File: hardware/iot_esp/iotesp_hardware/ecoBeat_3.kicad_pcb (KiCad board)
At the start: 2 copper layers, 67.6 x 58.6 mm, 10 parts, among them J1 Test, P1 CONN_02X05, U1 WeMos_mini

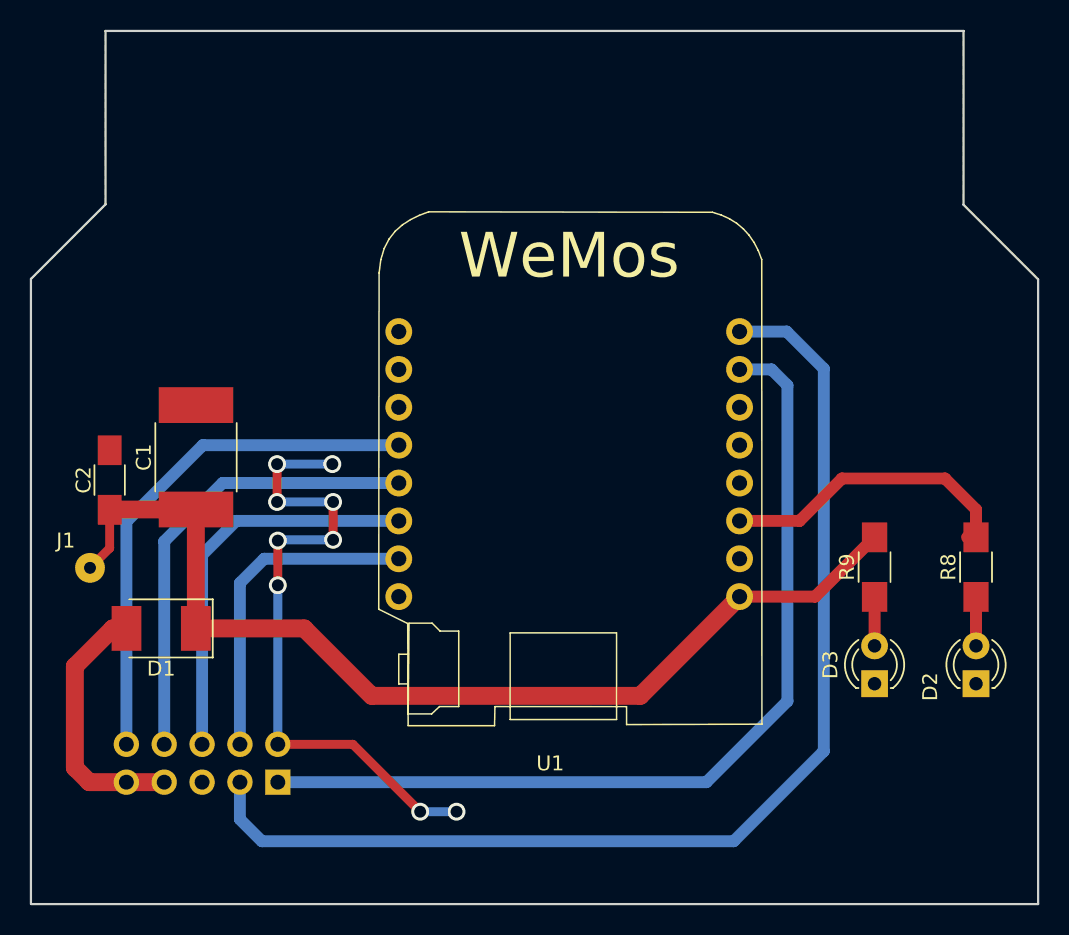
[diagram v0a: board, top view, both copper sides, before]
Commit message: iot-esp hw v3: side ventilation
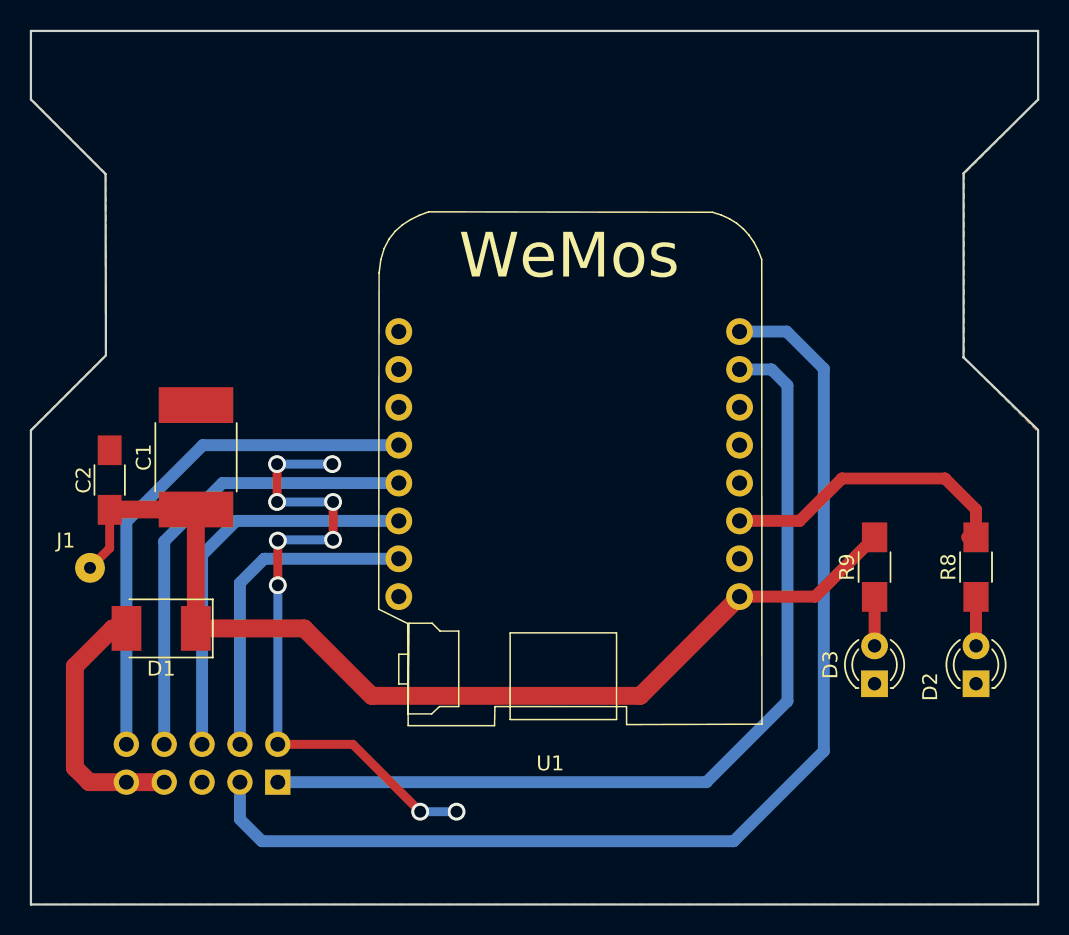
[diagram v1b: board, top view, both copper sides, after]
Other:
- outline, holes or cut-outs redrawn
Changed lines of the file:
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@@
-(kicad_pcb (version 4) (host pcbnew 4.0.7-e2-6376~61~ubuntu18.04.1)
+(kicad_pcb (version 20171130) (host pcbnew 5.0.2+dfsg1-1)
   (general
-    (links 22)
-    (no_connects 0)
-    (area 28.014801 19.652 132.9196 109.329201)
     (thickness 1.6)
-    (drawings 29)
+    (drawings 36)
     (tracks 72)
     (zones 0)
@@
   )
   (layers
-    (0 F.Cu signal hide)
-    (31 B.Cu signal hide)
+    (0 F.Cu signal)
+    (31 B.Cu signal)
     (32 B.Adhes user)
     (33 F.Adhes user)
@@
     (42 Eco1.User user)
     (43 Eco2.User user)
-    (44 Edge.Cuts user)
+    (44 Edge.Cuts user hide)
     (45 Margin user)
     (46 B.CrtYd user)
@@
     (pad_drill 1)
     (pad_to_mask_clearance 0.2)
+    (solder_mask_min_width 0.25)
     (aux_axis_origin 0 0)
     (grid_origin 221.6404 115.9764)
@@
       (layerselection 0x3d0f0_80000001)
       (usegerberextensions false)
+      (usegerberattributes false)
+      (usegerberadvancedattributes false)
+      (creategerberjobfile false)
       (excludeedgelayer true)
       (linewidth 0.100000)
@@
       (hpglpennumber 1)
       (hpglpenspeed 20)
-      (hpglpendiameter 15)
-      (hpglpenoverlay 2)
+      (hpglpendiameter 15.000000)
       (psnegative false)
       (psa4output false)
@@
       (drillshape 0)
       (scaleselection 1)
-      (outputdirectory /home/onsar/onsar_git/onsar/ecopower/hardware/iot_esp/iotesp_hardware/gerber/))
+      (outputdirectory "/home/onsar/onsar_git/onsar/ecopower/hardware/iot_esp/iotesp_hardware/gerber/"))
   )
   (net 0 "")
@@
       (effects (font (size 1 1) (thickness 0.15)) (justify mirror))
     )
-    (fp_text value CONN_02X05 (at 4.445 -4.445 360) (layer B.Fab)
+    (fp_text value CONN_02X05 (at 4.445 -4.445) (layer B.Fab)
       (effects (font (size 1 1) (thickness 0.15)) (justify mirror))
     )
@@
     (fp_line (start -1.33 0) (end -1.33 1.33) (layer B.SilkS) (width 0.12))
     (fp_line (start -1.33 1.33) (end 0 1.33) (layer B.SilkS) (width 0.12))
-    (fp_text user %R (at -2.3622 -0.762 360) (layer B.Fab)
+    (fp_text user %R (at -2.3622 -0.762) (layer B.Fab)
       (effects (font (size 1 1) (thickness 0.15)) (justify mirror))
     )
@@
     )
   )
-  (gr_line (start 50.0634 31.3436) (end 107.6198 31.3436) (angle 90) (layer Edge.Cuts) (width 0.15))
-  (gr_line (start 45.0596 47.9806) (end 45.0596 89.8906) (angle 90) (layer Edge.Cuts) (width 0.15))
-  (gr_line (start 50.0634 42.9768) (end 45.0596 47.9806) (angle 90) (layer Edge.Cuts) (width 0.15))
-  (gr_line (start 50.0634 31.3436) (end 50.0634 42.9768) (angle 90) (layer Edge.Cuts) (width 0.15))
-  (gr_line (start 112.6236 48.006) (end 112.6236 89.916) (angle 90) (layer Edge.Cuts) (width 0.15))
-  (gr_line (start 107.6198 43.0022) (end 112.6236 48.006) (angle 90) (layer Edge.Cuts) (width 0.15))
-  (gr_line (start 107.6198 31.3436) (end 107.6198 43.0022) (angle 90) (layer Edge.Cuts) (width 0.15))
+  (gr_line (start 112.6236 58.1152) (end 107.6198 53.2384) (layer Edge.Cuts) (width 0.15))
+  (gr_line (start 107.6198 40.9194) (end 107.6198 53.2638) (layer Edge.Cuts) (width 0.15))
+  (gr_line (start 50.0888 53.1114) (end 45.0596 58.1406) (layer Edge.Cuts) (width 0.15))
+  (gr_line (start 50.0634 40.9448) (end 50.0888 53.086) (layer Edge.Cuts) (width 0.15))
+  (gr_line (start 50.038 40.9194) (end 107.5436 40.9194) (layer Dwgs.User) (width 0.2))
+  (gr_line (start 50.0634 53.2384) (end 107.5944 53.2638) (layer Dwgs.User) (width 0.2))
+  (gr_line (start 45.0596 35.941) (end 50.0634 40.9448) (layer Edge.Cuts) (width 0.15))
+  (gr_line (start 112.6236 35.941) (end 107.6198 40.894) (layer Edge.Cuts) (width 0.15))
+  (gr_line (start 45.0596 89.9414) (end 112.6236 89.9414) (layer Edge.Cuts) (width 0.15))
+  (gr_line (start 45.0596 58.1406) (end 45.0596 89.9414) (layer Edge.Cuts) (width 0.15))
+  (gr_line (start 45.0596 31.3436) (end 45.0596 35.941) (layer Edge.Cuts) (width 0.15))
+  (gr_line (start 112.6236 31.3436) (end 45.0596 31.3436) (layer Edge.Cuts) (width 0.15))
+  (gr_line (start 112.6236 35.9664) (end 112.6236 31.3436) (layer Edge.Cuts) (width 0.15))
+  (gr_line (start 112.6236 89.916) (end 112.6236 58.1406) (layer Edge.Cuts) (width 0.15))
+  (gr_line (start 34.9504 35.9664) (end 126.3904 35.9664) (layer Dwgs.User) (width 0.2))
+  (gr_line (start 33.6804 58.1279) (end 127.5969 58.1279) (layer Dwgs.User) (width 0.2))
   (dimension 5.0038 (width 0.3) (layer Dwgs.User)
     (gr_text "5,004 mm" (at 110.1217 21.002) (layer Dwgs.User)
@@
     (arrow2b (pts (xy 51.4604 96.5708) (xy 50.333896 97.157221)))
   )
-  (gr_line (start 45.0596 89.916) (end 112.6236 89.916) (angle 90) (layer Edge.Cuts) (width 0.15))
   (dimension 11.0236 (width 0.3) (layer Dwgs.User)
     (gr_text "11,024 mm" (at 107.1626 85.0176) (layer Dwgs.User)
@@
   (gr_line (start 128.3208 78.232) (end 128.3208 78.2828) (angle 90) (layer Dwgs.User) (width 0.2))
   (gr_line (start 45.0596 78.232) (end 128.3208 78.232) (angle 90) (layer Dwgs.User) (width 0.2))
-  (gr_line (start 45.0596 43.0276) (end 127.508 43.0276) (angle 90) (layer Dwgs.User) (width 0.2))
   (dimension 17.6276 (width 0.3) (layer Dwgs.User)
     (gr_text "17,628 mm" (at 40.1536 69.469 270) (layer Dwgs.User)
@@
     (polygon
       (pts
-        (xy 107.6198 43.0022) (xy 112.6236 48.006) (xy 112.6236 89.916) (xy 45.0596 89.916) (xy 45.0596 47.9806)
-        (xy 50.0634 42.9768) (xy 50.0634 31.3436) (xy 107.6198 31.3436)
+        (xy 45.0596 31.3436) (xy 112.6236 31.3436) (xy 112.6236 35.9664) (xy 107.6706 40.9194) (xy 107.6706 53.2892)
+        (xy 112.6236 58.2422) (xy 112.6236 89.9414) (xy 45.0596 89.9414) (xy 45.0596 58.1152) (xy 50.0888 53.1114)
+        (xy 50.0634 40.894) (xy 45.0596 35.8902) (xy 45.0596 31.4452)
       )
     )
@@
     (polygon
       (pts
-        (xy 107.6198 43.0022) (xy 112.6236 48.006) (xy 112.6236 89.916) (xy 45.0596 89.916) (xy 45.0596 47.9806)
-        (xy 50.0634 42.9768) (xy 50.0634 31.3436) (xy 107.6198 31.3436)
+        (xy 45.0596 31.3436) (xy 112.6236 31.3436) (xy 112.6236 35.9664) (xy 107.6706 40.9194) (xy 107.6706 53.2892)
+        (xy 112.6236 58.2422) (xy 112.6236 89.9414) (xy 45.0596 89.9414) (xy 45.0596 58.1152) (xy 50.0888 53.086)
+        (xy 50.0888 40.9194) (xy 45.0596 35.8902)
       )
     )
